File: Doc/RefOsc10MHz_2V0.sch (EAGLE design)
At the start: 74 parts, among them CON1 TYCO-AMP_USBUSB-B_SMT, CON11 MCX-J-P-X-RA-SM1, CON2 HEADER-2X5SMD, CON3 SD-73100-0105, CON4 AVR-ISP-10SMD, CON5 AVR-JTAG-10SMD, CON6 HEADER-2X3SMD, IC1 ATmega328-P, IC11 712-RXM-GNSS-TM-B, IC2 LC4032V_XXT44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

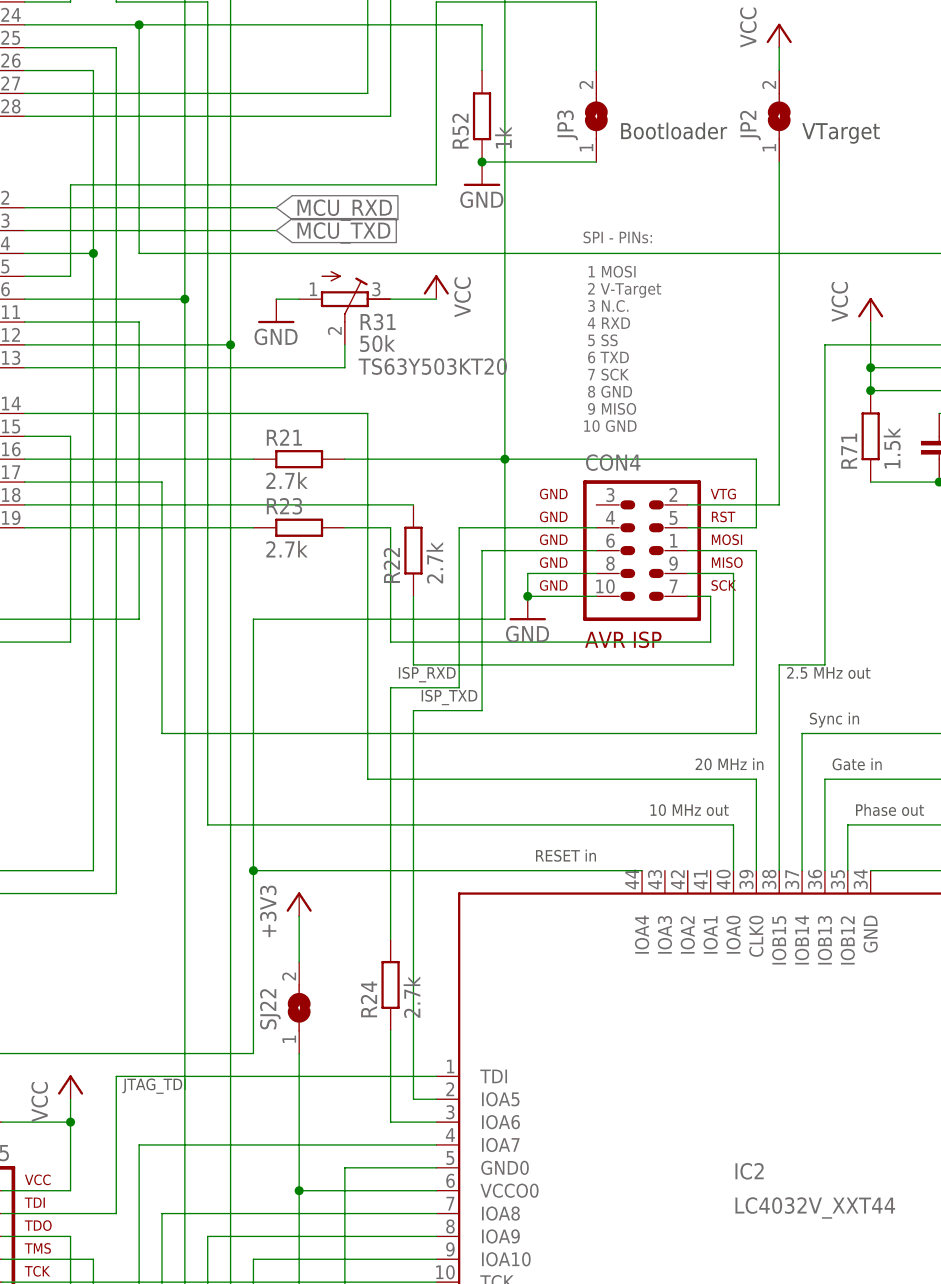
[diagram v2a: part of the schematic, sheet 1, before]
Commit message: avr_DF4IAH_Bootloader - Doc - Eagle: ISP-Connector changed from old 10 to new 6 pin variant
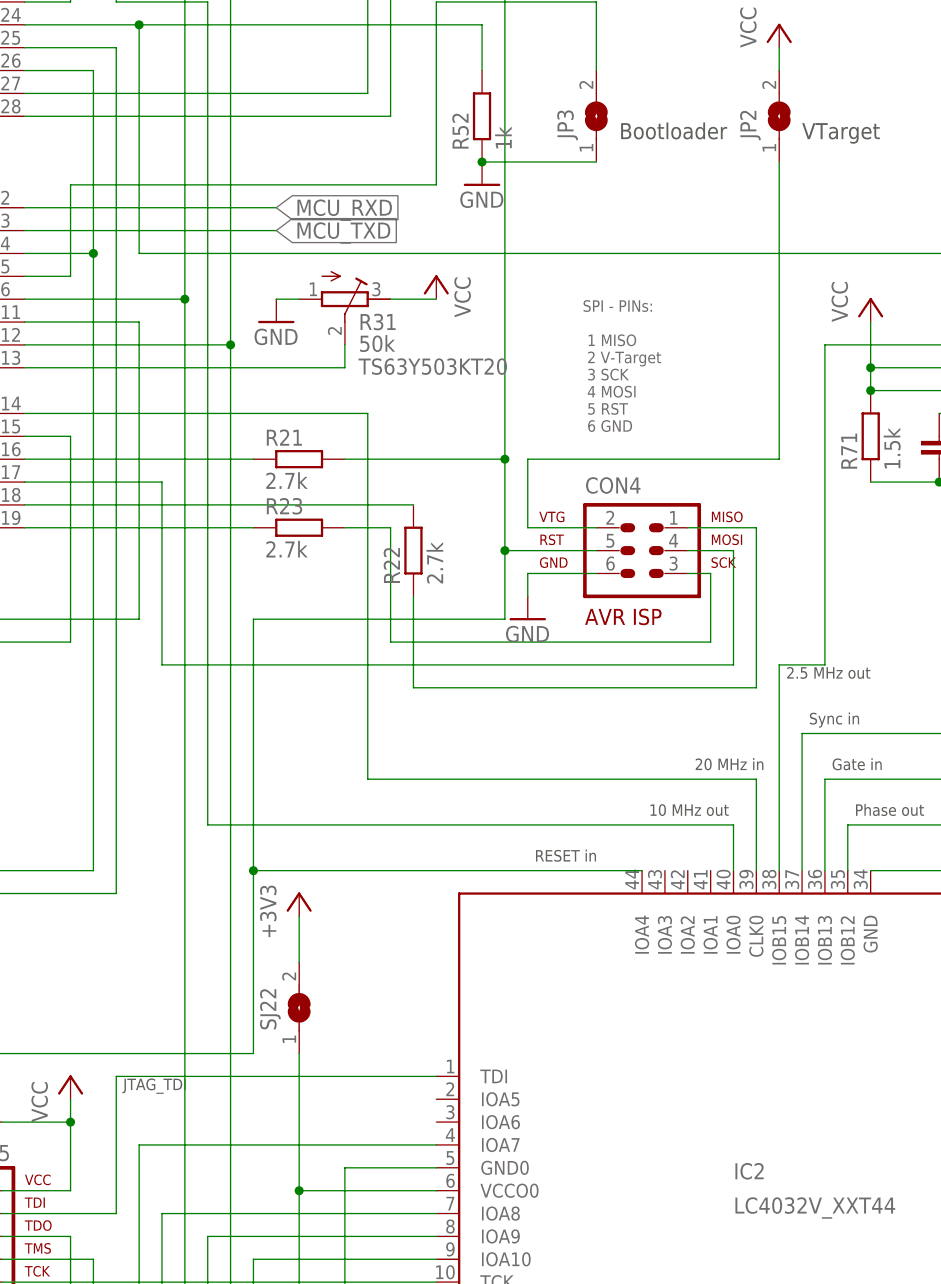
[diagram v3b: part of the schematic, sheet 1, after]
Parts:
- removed R24: 2.7k, rcl:R-EU_R0805
- CON4: value AVR-ISP-10SMD -> AVR-ISP-6SMD; device atmel-1:AVR-ISP-10SMD -> atmel-1:AVR-ISP-6SMD
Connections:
- removed net CPLD_ISP_RXD: IC2.IOA6, R24.1
- removed net ISP_RXD: CON4.4, R24.2
- removed net ISP_TXD: CON4.6, IC2.IOA5
- net GND: now also CON4.6; no longer CON4.10, CON4.8
- net ISP_MISO: now also CON4.1; no longer CON4.9
- net ISP_MOSI: now also CON4.4; no longer CON4.1
- net ISP_SCK: now also CON4.3; no longer CON4.7
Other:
- note added: "SPI - PINs: 1 MISO 2 V-Target 3 SCK 4 MOSI 5 RST 6 GND"
- note removed: "ISP_RXD"
- note removed: "ISP_TXD"
- note removed: "SPI - PINs: 1 MOSI 2 V-Target 3 N.C. 4 RXD 5 SS 6 TXD 7 SCK 8 GND 9 MISO 10 GND"
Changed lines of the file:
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@@
 <part name="R72" library="df4iah" deviceset="R-TRIMM" device="TS63Y" value="10k"/>
 <part name="GND6" library="supply1" deviceset="GND" device=""/>
-<part name="CON4" library="atmel-1" deviceset="AVR-ISP-10" device="SMD"/>
 <part name="CON2" library="df4iah" deviceset="HEADER-2X5" device="SMD"/>
 <part name="IC3" library="74xx-eu" deviceset="74*221" device="D" technology="HCT"/>
@@
 <part name="IC6" library="df4iah" deviceset="LM2831" device="" technology="YMF" value="LM2831YMF"/>
 <part name="D82" library="diode" deviceset="ZENER-DIODE" device="SOT23" value="CRS08"/>
-<part name="R24" library="rcl" deviceset="R-EU_" device="R0805" value="2.7k"/>
 <part name="R25" library="rcl" deviceset="R-EU_" device="R0805" value="2.7k"/>
 <part name="R221" library="rcl" deviceset="R-EU_" device="R0805" value="56"/>
@@
 <part name="CON3" library="df4iah" deviceset="MOLEX_BNC-JACK-50R_SD-73100-0105" device="" value="SD-73100-0105"/>
 <part name="CON1" library="df4iah" deviceset="TYCO-AMP_USB" device="USB-B_SMT"/>
+<part name="CON4" library="atmel-1" deviceset="AVR-ISP-6" device="SMD"/>
 </parts>
 <sheets>
@@
 <text x="107.696" y="83.058" size="1.778" layer="97">USB D+</text>
 <text x="181.356" y="137.668" size="1.27" layer="96" font="fixed">SPI - PINs:
- 1 MOSI
+ 1 MISO
  2 V-Target
- 3 N.C.
- 4 RXD
- 5 SS
- 6 TXD
- 7 SCK
- 8 GND
- 9 MISO
-10 GND</text>
+ 3 SCK
+ 4 MOSI
+ 5 RST
+ 6 GND</text>
 <text x="65.024" y="161.798" size="1.778" layer="97">NC</text>
 <text x="137.922" y="1.016" size="1.27" layer="97">10 kHz</text>
@@
 <text x="130.302" y="41.656" size="1.27" layer="97">JTAG_TCK</text>
 <text x="130.302" y="64.516" size="1.27" layer="97">JTAG_TDI</text>
-<text x="163.322" y="107.696" size="1.27" layer="97">ISP_TXD</text>
-<text x="160.782" y="110.236" size="1.27" layer="97">ISP_RXD</text>
 <text x="94.742" y="-14.224" size="1.27" layer="97">CPLD_SER_GPS</text>
 <text x="140.97" y="214.122" size="1.27" layer="96" font="fixed">I2C - PINs:
@@
 </instance>
 <instance part="GND6" gate="1" x="175.26" y="116.84"/>
-<instance part="CON4" gate="G$1" x="187.96" y="124.46"/>
 <instance part="CON2" gate="G$1" x="210.82" y="215.9"/>
 <instance part="IC3" gate="A" x="248.92" y="139.7"/>
@@
 <instance part="IC6" gate="A" x="35.56" y="238.76"/>
 <instance part="D82" gate="G$1" x="236.22" y="203.2" rot="R270"/>
-<instance part="R24" gate="G$1" x="160.02" y="76.2" rot="R90"/>
 <instance part="R25" gate="G$1" x="111.76" y="22.86"/>
 <instance part="R221" gate="G$1" x="86.36" y="241.3" smashed="yes" rot="R270">
@@
 <attribute name="NAME" x="16.51" y="96.52" size="1.778" layer="95"/>
 </instance>
+<instance part="CON4" gate="G$1" x="187.96" y="124.46"/>
 </instances>
 <busses>
@@
 <segment>
 <pinref part="GND6" gate="1" pin="GND"/>
-<wire x1="175.26" y1="119.38" x2="182.88" y2="119.38" width="0.1524" layer="91"/>
 <wire x1="175.26" y1="119.38" x2="175.26" y2="121.92" width="0.1524" layer="91"/>
 <wire x1="175.26" y1="121.92" x2="182.88" y2="121.92" width="0.1524" layer="91"/>
-<junction x="175.26" y="119.38"/>
-<pinref part="CON4" gate="G$1" pin="8"/>
-<pinref part="CON4" gate="G$1" pin="10"/>
+<pinref part="CON4" gate="G$1" pin="6"/>
 </segment>
 <segment>
@@
 <wire x1="160.02" y1="127" x2="160.02" y2="114.3" width="0.1524" layer="91"/>
 <wire x1="160.02" y1="114.3" x2="195.58" y2="114.3" width="0.1524" layer="91"/>
-<wire x1="195.58" y1="114.3" x2="195.58" y2="119.38" width="0.1524" layer="91"/>
-<wire x1="195.58" y1="119.38" x2="193.04" y2="119.38" width="0.1524" layer="91"/>
-<pinref part="CON4" gate="G$1" pin="7"/>
+<wire x1="195.58" y1="114.3" x2="195.58" y2="121.92" width="0.1524" layer="91"/>
 <pinref part="R23" gate="G$1" pin="2"/>
+<pinref part="CON4" gate="G$1" pin="3"/>
+<wire x1="195.58" y1="121.92" x2="193.04" y2="121.92" width="0.1524" layer="91"/>
 </segment>
 </net>
@@
 <net name="ISP_VTARGET" class="0">
 <segment>
-<wire x1="203.2" y1="129.54" x2="203.2" y2="167.64" width="0.1524" layer="91"/>
 <pinref part="JP2" gate="1" pin="1"/>
-<wire x1="203.2" y1="129.54" x2="193.04" y2="129.54" width="0.1524" layer="91"/>
 <pinref part="CON4" gate="G$1" pin="2"/>
+<wire x1="203.2" y1="134.62" x2="203.2" y2="167.64" width="0.1524" layer="91"/>
+<wire x1="182.88" y1="127" x2="175.26" y2="127" width="0.1524" layer="91"/>
+<wire x1="175.26" y1="127" x2="175.26" y2="134.62" width="0.1524" layer="91"/>
+<wire x1="175.26" y1="134.62" x2="203.2" y2="134.62" width="0.1524" layer="91"/>
 </segment>
 </net>
@@
 <net name="ISP_MISO" class="0">
 <segment>
-<wire x1="162.56" y1="111.76" x2="198.12" y2="111.76" width="0.1524" layer="91"/>
-<wire x1="198.12" y1="111.76" x2="198.12" y2="121.92" width="0.1524" layer="91"/>
-<wire x1="198.12" y1="121.92" x2="193.04" y2="121.92" width="0.1524" layer="91"/>
-<pinref part="CON4" gate="G$1" pin="9"/>
-<wire x1="162.56" y1="111.76" x2="162.56" y2="119.38" width="0.1524" layer="91"/>
+<wire x1="162.56" y1="109.22" x2="200.66" y2="109.22" width="0.1524" layer="91"/>
+<wire x1="162.56" y1="109.22" x2="162.56" y2="119.38" width="0.1524" layer="91"/>
 <pinref part="R22" gate="G$1" pin="1"/>
+<wire x1="200.66" y1="109.22" x2="200.66" y2="127" width="0.1524" layer="91"/>
+<pinref part="CON4" gate="G$1" pin="1"/>
+<wire x1="200.66" y1="127" x2="193.04" y2="127" width="0.1524" layer="91"/>
 </segment>
 </net>
 <net name="ISP_MOSI" class="0">
 <segment>
-<wire x1="193.04" y1="124.46" x2="200.66" y2="124.46" width="0.1524" layer="91"/>
-<wire x1="200.66" y1="124.46" x2="200.66" y2="104.14" width="0.1524" layer="91"/>
-<wire x1="200.66" y1="104.14" x2="134.62" y2="104.14" width="0.1524" layer="91"/>
-<wire x1="134.62" y1="104.14" x2="134.62" y2="132.08" width="0.1524" layer="91"/>
+<wire x1="193.04" y1="124.46" x2="198.12" y2="124.46" width="0.1524" layer="91"/>
+<wire x1="198.12" y1="124.46" x2="198.12" y2="111.76" width="0.1524" layer="91"/>
+<wire x1="198.12" y1="111.76" x2="134.62" y2="111.76" width="0.1524" layer="91"/>
+<wire x1="134.62" y1="111.76" x2="134.62" y2="132.08" width="0.1524" layer="91"/>
 <pinref part="IC1" gate="G$1" pin="PB3(MOSI/OC2)"/>
 <wire x1="134.62" y1="132.08" x2="119.38" y2="132.08" width="0.1524" layer="91"/>
-<pinref part="CON4" gate="G$1" pin="1"/>
+<pinref part="CON4" gate="G$1" pin="4"/>
 </segment>
 </net>
@@
 <wire x1="104.14" y1="198.12" x2="172.72" y2="198.12" width="0.1524" layer="91"/>
 <wire x1="154.94" y1="134.62" x2="172.72" y2="134.62" width="0.1524" layer="91"/>
-<wire x1="172.72" y1="134.62" x2="200.66" y2="134.62" width="0.1524" layer="91"/>
-<wire x1="200.66" y1="134.62" x2="200.66" y2="127" width="0.1524" layer="91"/>
-<wire x1="200.66" y1="127" x2="193.04" y2="127" width="0.1524" layer="91"/>
-<pinref part="CON4" gate="G$1" pin="5"/>
 <wire x1="172.72" y1="198.12" x2="172.72" y2="134.62" width="0.1524" layer="91"/>
 <junction x="172.72" y="134.62"/>
-<wire x1="172.72" y1="134.62" x2="172.72" y2="116.84" width="0.1524" layer="91"/>
+<wire x1="172.72" y1="134.62" x2="172.72" y2="124.46" width="0.1524" layer="91"/>
+<wire x1="172.72" y1="124.46" x2="172.72" y2="116.84" width="0.1524" layer="91"/>
 <wire x1="172.72" y1="116.84" x2="144.78" y2="116.84" width="0.1524" layer="91"/>
 <wire x1="144.78" y1="116.84" x2="144.78" y2="88.9" width="0.1524" layer="91"/>
@@
 <wire x1="144.78" y1="88.9" x2="187.96" y2="88.9" width="0.1524" layer="91"/>
 <junction x="144.78" y="88.9"/>
+<pinref part="CON4" gate="G$1" pin="5"/>
+<wire x1="172.72" y1="124.46" x2="182.88" y2="124.46" width="0.1524" layer="91"/>
+<junction x="172.72" y="124.46"/>
 </segment>
 </net>
@@
 </segment>
 </net>
-<net name="ISP_RXD" class="0">
-<segment>
-<pinref part="CON4" gate="G$1" pin="4"/>
-<wire x1="182.88" y1="127" x2="167.64" y2="127" width="0.1524" layer="91"/>
-<wire x1="167.64" y1="127" x2="167.64" y2="109.22" width="0.1524" layer="91"/>
-<wire x1="167.64" y1="109.22" x2="160.02" y2="109.22" width="0.1524" layer="91"/>
-<wire x1="160.02" y1="109.22" x2="160.02" y2="81.28" width="0.1524" layer="91"/>
-<pinref part="R24" gate="G$1" pin="2"/>
-</segment>
-</net>
-<net name="ISP_TXD" class="0">
-<segment>
-<pinref part="CON4" gate="G$1" pin="6"/>
-<wire x1="182.88" y1="124.46" x2="170.18" y2="124.46" width="0.1524" layer="91"/>
-<wire x1="170.18" y1="124.46" x2="170.18" y2="106.68" width="0.1524" layer="91"/>
-<wire x1="170.18" y1="106.68" x2="162.56" y2="106.68" width="0.1524" layer="91"/>
-<wire x1="162.56" y1="106.68" x2="162.56" y2="63.5" width="0.1524" layer="91"/>
-<pinref part="IC2" gate="G$1" pin="IOA5"/>
-<wire x1="162.56" y1="63.5" x2="165.1" y2="63.5" width="0.1524" layer="91"/>
-</segment>
-</net>
-<net name="CPLD_ISP_RXD" class="0">
-<segment>
-<pinref part="IC2" gate="G$1" pin="IOA6"/>
-<pinref part="R24" gate="G$1" pin="1"/>
-<wire x1="165.1" y1="60.96" x2="160.02" y2="60.96" width="0.1524" layer="91"/>
-<wire x1="160.02" y1="60.96" x2="160.02" y2="71.12" width="0.1524" layer="91"/>
-</segment>
-</net>
